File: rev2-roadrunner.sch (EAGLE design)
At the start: 22 parts, among them J1 USB_MINI-B_SMT, Y1 16MHz

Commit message: Finalized Board and Schematic design
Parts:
- added C4: 0.1uF, SparkFun-Capacitors:1.0UF-1206-50V-10%
- added C5: 1.0uF, SparkFun-Capacitors:1.0UF-1206-50V-10%
- added D4: WS2812B, SparkFun-LED:WS2812B
- added F1: 6V/0.5A, SparkFun-Fuses:PPTC_HALF-AMP
- D7: value GREEN -> Yellow; device SparkFun-LED:LED-GREEN1206 -> SparkFun-LED:LED-YELLOWLILYPAD
- J2: device SparkFun-Connectors:CONN_03 -> SparkFun-Connectors:CONN_07
- J3: device SparkFun-Connectors:CONN_14 -> SparkFun-Connectors:CONN_10"
- J4: device SparkFun-Connectors:CONN_04 -> SparkFun-Connectors:CONN_06SILK_FEMALE_PTH
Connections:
- net USBD1_N renamed USB_D1_N
- net USBD1_P renamed USB_D1_P
- net USBD_N renamed USB_D_N
- net USBD_P renamed USB_D_P
- new net N$4: D3.A, F1.2
- new net USB_VCC: F1.1, J1.VBUS
- net 5V: now also C2.1, C4.1, C5.1, D2.A, D4.VDD, D7.A, J2.7, R3.2; no longer C2.2, J1.VBUS, J3.14, R7.2
- net AREF: now also J2.5; no longer J3.12
- net GND: now also C2.2, C4.2, C5.2, D4.VSS, J2.6; no longer C2.1, D2.C, D3.A, D7.C, J3.13
- net N$2: now also D7.C, R7.1; no longer D2.A, R2.1
- net N$3: now also D2.C, R2.2; no longer D7.A, R7.1
- net PB4: now also J3.4; no longer J3.1
- net PB5: now also J3.5; no longer J3.2
- net PB6: now also J3.6; no longer J3.3
- net PB7: now also J4.6
- net PC6: now also J3.7; no longer J3.4
- net PC7: now also J3.8; no longer J3.5
- net PD4: now also J3.1; no longer J2.1
- net PD6: now also J3.2; no longer J2.2
- net PD7: now also J3.3; no longer J2.3
- net PE6: now also J4.5
- net PF0: now also J2.4; no longer J3.11
- net PF1: now also J2.3; no longer J3.10
- net PF4: now also J2.2; no longer J3.9
- net PF5: now also J2.1; no longer J3.8
- net PF6: now also J3.10; no longer J3.7
- net PF7: now also D4.DI, J3.9; no longer J3.6
- net RX_LED: now also R2.1; no longer R2.2
- net TX_LED: now also R7.2; no longer R3.2
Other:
- note added: "IO LEDs"
- note added: "Int USB Cap"
- note added: "Programming Headers"
- note added: "USB Data"
- note added: "USB Power"
- note removed: "LEDs"
- note removed: "Programming"
- moved on the sheet: C1, C2, C3, C6, D1, D2, D3, D7, ICSP, J1, R1, R2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

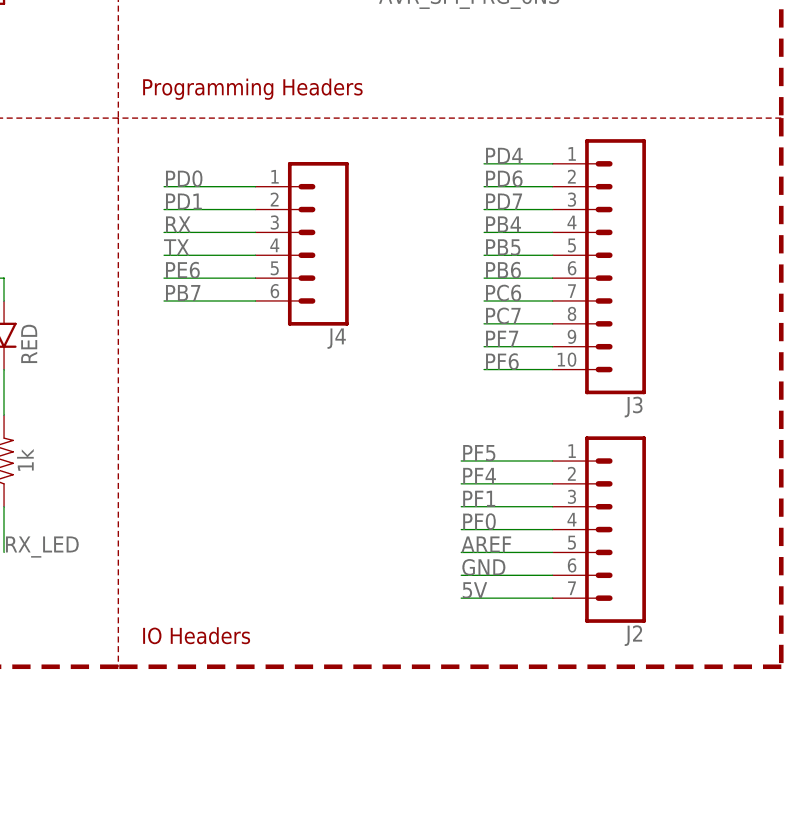
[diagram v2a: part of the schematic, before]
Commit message: Re-routed by hand + Moved C1 down
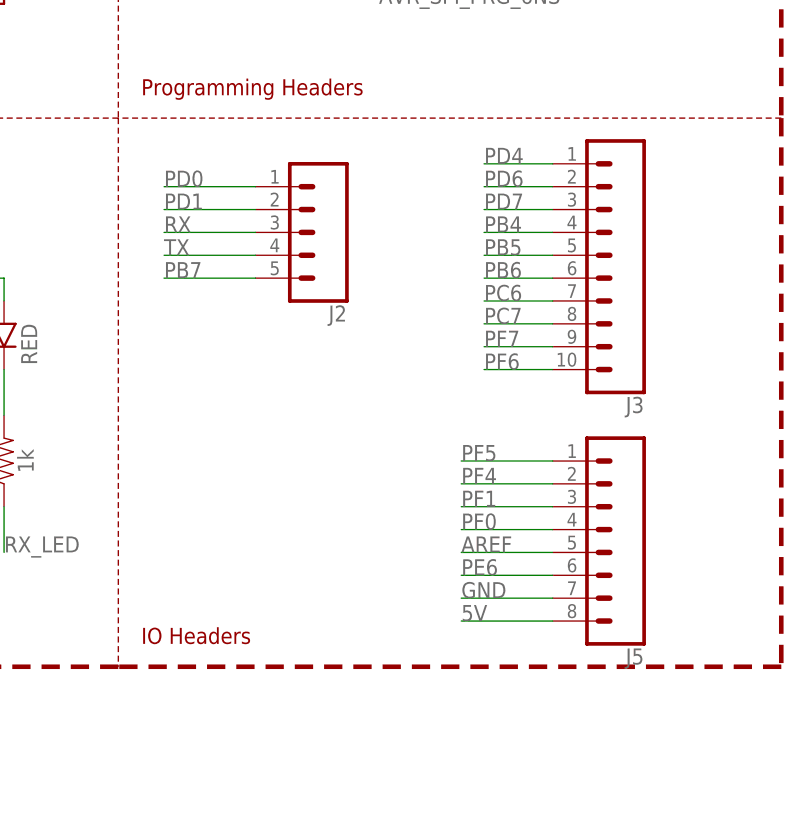
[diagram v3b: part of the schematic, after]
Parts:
- removed J4: (no value), SparkFun-Connectors:CONN_06SILK_FEMALE_PTH
- added J5: (no value), SparkFun-Connectors:CONN_08"
- J2: device SparkFun-Connectors:CONN_07 -> SparkFun-Connectors:CONN_05
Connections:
- net 5V: now also J5.8; no longer J2.7
- net AREF: now also J5.5; no longer J2.5
- net GND: now also J5.7; no longer J2.6
- net PB7: now also J2.5; no longer J4.6
- net PD0: now also J2.1; no longer J4.1
- net PD1: now also J2.2; no longer J4.2
- net PE6: now also J5.6; no longer J4.5
- net PF0: now also J5.4; no longer J2.4
- net PF1: now also J5.3; no longer J2.3
- net PF4: now also J5.2; no longer J2.2
- net PF5: now also J5.1; no longer J2.1
- net RX: now also J2.3; no longer J4.3
- net TX: now also J2.4; no longer J4.4
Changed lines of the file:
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@@
 <part name="GND4" library="SparkFun-PowerSymbols" library_urn="urn:adsk.eagle:library:530" deviceset="GND" device=""/>
 <part name="SUPPLY2" library="SparkFun-PowerSymbols" library_urn="urn:adsk.eagle:library:530" deviceset="5V" device=""/>
-<part name="J2" library="SparkFun-Connectors" deviceset="CONN_07" device=""/>
 <part name="D4" library="SparkFun-LED" deviceset="WS2812B" device="" value="WS2812B"/>
 <part name="J3" library="SparkFun-Connectors" deviceset="CONN_10" device="&quot;"/>
 <part name="SUPPLY5" library="SparkFun-PowerSymbols" library_urn="urn:adsk.eagle:library:530" deviceset="5V" device=""/>
 <part name="GND5" library="SparkFun-PowerSymbols" library_urn="urn:adsk.eagle:library:530" deviceset="GND" device=""/>
-<part name="J4" library="SparkFun-Connectors" deviceset="CONN_06" device="SILK_FEMALE_PTH"/>
+<part name="J5" library="SparkFun-Connectors" deviceset="CONN_08" device="&quot;"/>
+<part name="J2" library="SparkFun-Connectors" deviceset="CONN_05" device=""/>
 </parts>
 <sheets>
@@
 <instance part="GND4" gate="1" x="35.56" y="33.02"/>
 <instance part="SUPPLY2" gate="G$1" x="35.56" y="48.26"/>
-<instance part="J2" gate="G$1" x="205.74" y="73.66" rot="R180"/>
 <instance part="D4" gate="G$1" x="129.54" y="134.62"/>
 <instance part="J3" gate="G$1" x="210.82" y="93.98" rot="R180"/>
 <instance part="SUPPLY5" gate="G$1" x="114.3" y="142.24"/>
 <instance part="GND5" gate="1" x="114.3" y="124.46"/>
-<instance part="J4" gate="G$1" x="172.72" y="104.14" rot="R180"/>
+<instance part="J5" gate="G$1" x="205.74" y="71.12" rot="R180"/>
+<instance part="J2" gate="G$1" x="175.26" y="104.14" rot="R180"/>
 </instances>
 <busses>
@@
 </segment>
 <segment>
-<wire x1="200.66" y1="66.04" x2="190.5" y2="66.04" width="0.1524" layer="91"/>
-<label x="190.5" y="66.04" size="1.778" layer="95"/>
-<pinref part="J2" gate="G$1" pin="6"/>
+<wire x1="200.66" y1="63.5" x2="190.5" y2="63.5" width="0.1524" layer="91"/>
+<label x="190.5" y="63.5" size="1.778" layer="95"/>
+<pinref part="J5" gate="G$1" pin="7"/>
 </segment>
 <segment>
@@
 <wire x1="200.66" y1="68.58" x2="190.5" y2="68.58" width="0.1524" layer="91"/>
 <label x="190.5" y="68.58" size="1.778" layer="95"/>
-<pinref part="J2" gate="G$1" pin="5"/>
+<pinref part="J5" gate="G$1" pin="5"/>
 </segment>
 </net>
@@
 </segment>
 <segment>
-<wire x1="200.66" y1="63.5" x2="190.5" y2="63.5" width="0.1524" layer="91"/>
-<label x="190.5" y="63.5" size="1.778" layer="95"/>
-<pinref part="J2" gate="G$1" pin="7"/>
+<wire x1="200.66" y1="60.96" x2="190.5" y2="60.96" width="0.1524" layer="91"/>
+<label x="190.5" y="60.96" size="1.778" layer="95"/>
+<pinref part="J5" gate="G$1" pin="8"/>
 </segment>
 <segment>
@@
 <label x="157.48" y="106.68" size="1.778" layer="95"/>
 <wire x1="157.48" y1="106.68" x2="167.64" y2="106.68" width="0.1524" layer="91"/>
-<pinref part="J4" gate="G$1" pin="2"/>
+<pinref part="J2" gate="G$1" pin="2"/>
 </segment>
 </net>
@@
 <label x="157.48" y="109.22" size="1.778" layer="95"/>
 <wire x1="167.64" y1="109.22" x2="157.48" y2="109.22" width="0.1524" layer="91"/>
-<pinref part="J4" gate="G$1" pin="1"/>
+<pinref part="J2" gate="G$1" pin="1"/>
 </segment>
 </net>
@@
 </segment>
 <segment>
-<wire x1="167.64" y1="99.06" x2="157.48" y2="99.06" width="0.1524" layer="91"/>
-<label x="157.48" y="99.06" size="1.778" layer="95"/>
-<pinref part="J4" gate="G$1" pin="5"/>
+<wire x1="190.5" y1="66.04" x2="200.66" y2="66.04" width="0.1524" layer="91"/>
+<label x="190.5" y="66.04" size="1.778" layer="95"/>
+<pinref part="J5" gate="G$1" pin="6"/>
 </segment>
 </net>
@@
 </segment>
 <segment>
-<wire x1="167.64" y1="96.52" x2="157.48" y2="96.52" width="0.1524" layer="91"/>
-<label x="157.48" y="96.52" size="1.778" layer="95"/>
-<pinref part="J4" gate="G$1" pin="6"/>
+<wire x1="167.64" y1="99.06" x2="157.48" y2="99.06" width="0.1524" layer="91"/>
+<label x="157.48" y="99.06" size="1.778" layer="95"/>
+<pinref part="J2" gate="G$1" pin="5"/>
 </segment>
 </net>
@@
 <wire x1="200.66" y1="78.74" x2="190.5" y2="78.74" width="0.1524" layer="91"/>
 <label x="190.5" y="78.74" size="1.778" layer="95"/>
-<pinref part="J2" gate="G$1" pin="1"/>
+<pinref part="J5" gate="G$1" pin="1"/>
 </segment>
 </net>
@@
 <wire x1="200.66" y1="76.2" x2="190.5" y2="76.2" width="0.1524" layer="91"/>
 <label x="190.5" y="76.2" size="1.778" layer="95"/>
-<pinref part="J2" gate="G$1" pin="2"/>
+<pinref part="J5" gate="G$1" pin="2"/>
 </segment>
 </net>
@@
 <wire x1="200.66" y1="73.66" x2="190.5" y2="73.66" width="0.1524" layer="91"/>
 <label x="190.5" y="73.66" size="1.778" layer="95"/>
-<pinref part="J2" gate="G$1" pin="3"/>
+<pinref part="J5" gate="G$1" pin="3"/>
 </segment>
 </net>
@@
 <wire x1="200.66" y1="71.12" x2="190.5" y2="71.12" width="0.1524" layer="91"/>
 <label x="190.5" y="71.12" size="1.778" layer="95"/>
-<pinref part="J2" gate="G$1" pin="4"/>
+<pinref part="J5" gate="G$1" pin="4"/>
 </segment>
 </net>
@@
 <wire x1="167.64" y1="104.14" x2="157.48" y2="104.14" width="0.1524" layer="91"/>
 <label x="157.48" y="104.14" size="1.778" layer="95"/>
-<pinref part="J4" gate="G$1" pin="3"/>
+<pinref part="J2" gate="G$1" pin="3"/>
 </segment>
 </net>
@@
 <wire x1="167.64" y1="101.6" x2="157.48" y2="101.6" width="0.1524" layer="91"/>
 <label x="157.48" y="101.6" size="1.778" layer="95"/>
-<pinref part="J4" gate="G$1" pin="4"/>
-</segment>
-</net>
+<pinref part="J2" gate="G$1" pin="4"/>
+</segment>
+</net>
